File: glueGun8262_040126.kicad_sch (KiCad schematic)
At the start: 63 parts, among them CN1 KF243-5.0-2P, CN2 KF243-5.0-2P, CN3 KF243-5.0-2P, CN4 KF243-5.0-2P, CN5 KF243-5.0-2P, CN6 KF243-5.0-2P, CN7 KF243-5.0-2P, CN9 KF243-5.0-4P, J1 Conn_01x22_Socket, U1 DRV8262DDWR, U10 INA240A2DR, U11 INA240A2DR, U2 DRV8262DDWR, U3 ESP32-S3-DEVKITC-1-N8R2, U5 6N137, U6 INA240A2DR, U7 INA240A2DR, U8 K7805-1000R3_C2992391, U9 TLP281-4(GB-TP,J,F

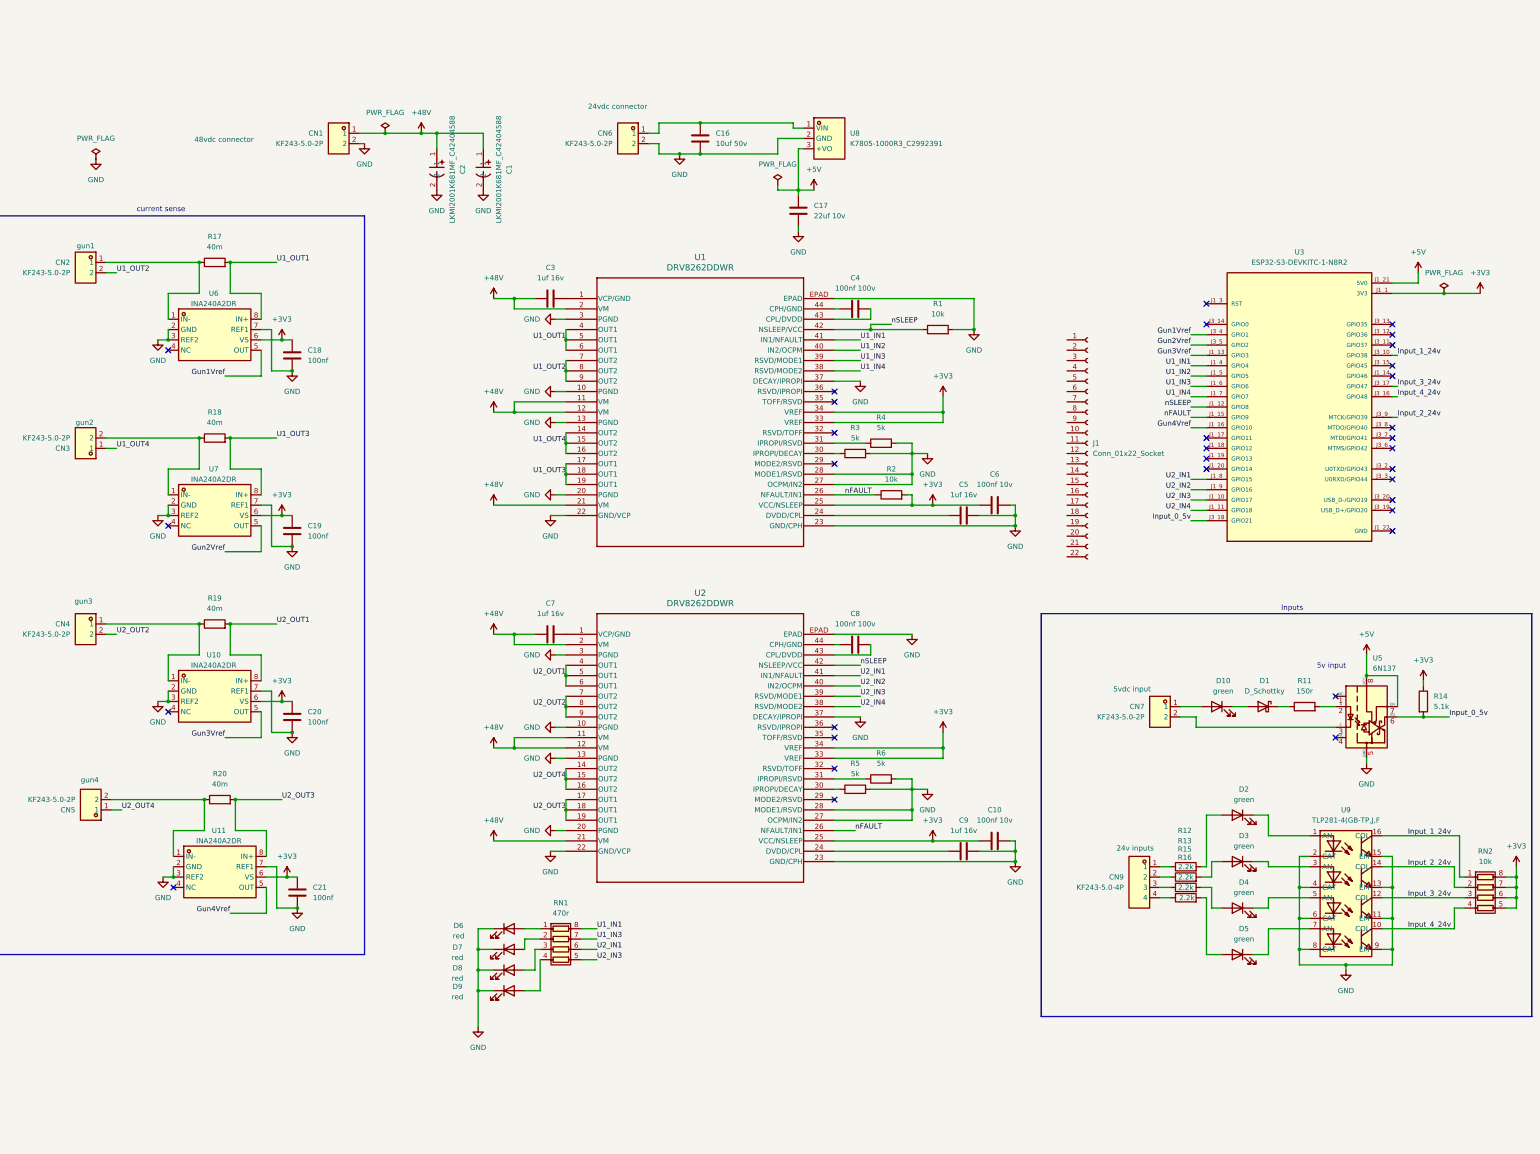
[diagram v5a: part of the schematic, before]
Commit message: added mounting holes
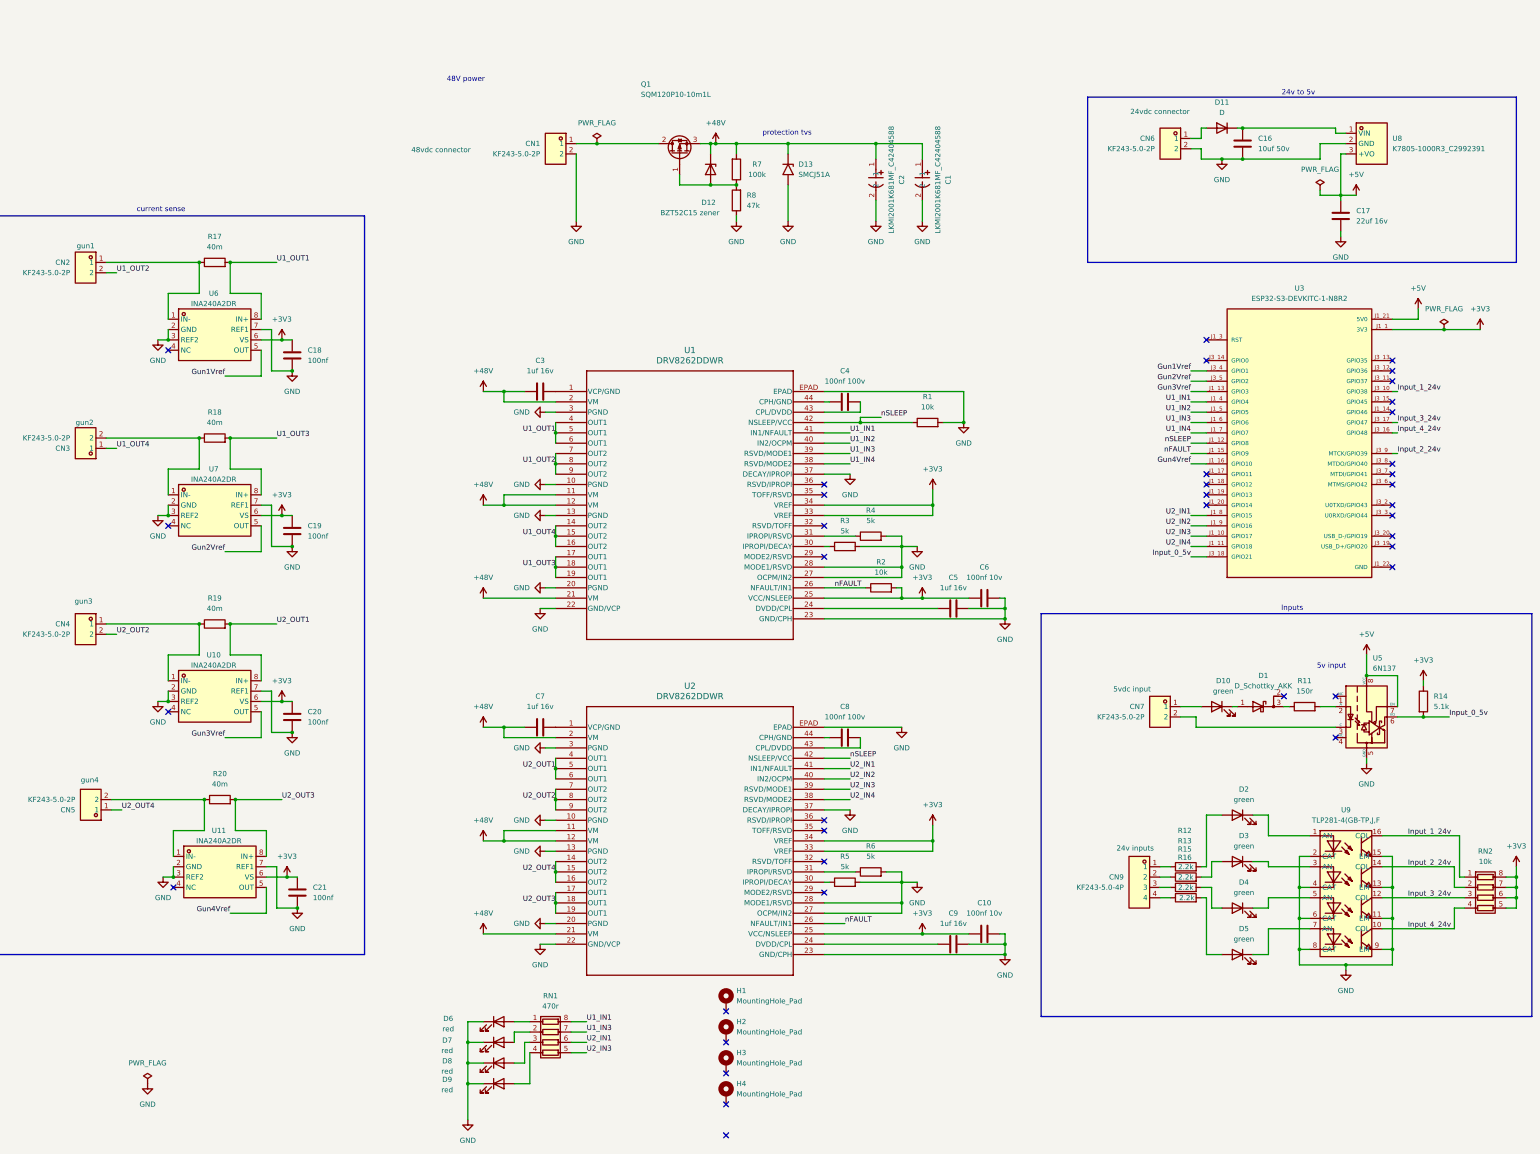
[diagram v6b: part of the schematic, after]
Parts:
- removed D1: D_Schottky, Package_TO_SOT_SMD:SOT-23, symbol Device:D_Schottky
- removed J1: Conn_01x22_Socket, symbol Connector:Conn_01x22_Socket
- added D1: D_Schottky_AKK, Package_TO_SOT_SMD:SOT-23, symbol Device:D_Schottky_AKK
- added D11: D, Diode_SMD:D_SMA, symbol Device:D
- added D12: BZT52C15 zener, Diode_SMD:D_SOD-123, symbol Device:D_Zener
- added D13: SMCJ51A, Diode_SMD:D_SMC, symbol Diode:SMAJ51A
- added H1, H2, H3, H4: MountingHole_Pad, MountingHole:MountingHole_3.2mm_M3_Pad, symbol Mechanical:MountingHole_Pad
- added Q1: SQM120P10-10m1L, Package_TO_SOT_SMD:TO-263-2, symbol Transistor_FET:Q_PMOS_GDS
- added R7: 100k, Resistor_SMD:R_0805_2012Metric, symbol Device:R
- added R8: 47k, Resistor_SMD:R_0805_2012Metric, symbol Device:R
- C17: value 22uf 10v -> 22uf 16v; lcsc C723738 -> C513771
- U1, U2: footprint HTSSOP44-DDW_TEX -> DRV8262DDWR:HTSSOP44-DDW_TEX
- U5: footprint Package_DIP:DIP-8_W7.62mm -> Package_DIP:SMDIP-8_W9.53mm
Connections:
- net +48V: now also D12.1 (K), D13.1 (A1), Q1.3 (S), R7.2; no longer CN1.1
- net GND: now also D13.2 (A2), R8.1
- net at R11.1: now also D1.3 (K)
- net at D10.1 (K): now also D1.1 (A)
- net at C16.1, U8.1 (VIN): now also D11.1 (K); no longer CN6.1
- new net: D12.2 (A), Q1.1 (G), R7.1, R8.2
- new net: CN1.1, Q1.2 (D)
- new net: CN6.1, D11.2 (A)
- no-connect marks 33 -> 39
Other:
- note added: "24v to 5v"
- note added: "48V power"
- note added: "protection tvs"
- moved on the sheet: C1, C10, C16, C17, C2, C3, C4, C5, C6, C7, C8, C9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

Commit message: saved
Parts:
- added D14: D_Schottky, symbol Device:D_Schottky
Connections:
- net +5V: now also D14.1 (K); no longer C17.1, U8.3 (+VO)
- new net: C17.1, D14.2 (A), U8.3 (+VO)
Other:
- moved on the sheet: C16, C17, CN6, D11, U8
